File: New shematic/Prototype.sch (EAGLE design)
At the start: 15 parts, among them SW1 1-1825910-4, U1 BOB-12009, U3 NUCLEO-L432KC, U4 24AA64T-I/OT

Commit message: remaked the pcb board
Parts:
- removed JP2, JP3: (no value), pinhead:PINHD-1X1
- added SV2: (no value), con-lstb:MA04-1
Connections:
- removed net N$9: JP2.1, U1.LV, U3G$2.VIN
- new net N$18: SV2.1, SV2.2, U1.LV, U3G$2.VIN
- net GND: now also SV2.3, SV2.4; no longer JP3.1
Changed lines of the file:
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@@
 <part name="GND2" library="supply1" library_urn="urn:adsk.eagle:library:371" deviceset="GND" device=""/>
 <part name="U4" library="24AA64" deviceset="24AA64T-I/OT" device=""/>
-<part name="JP2" library="pinhead" library_urn="urn:adsk.eagle:library:325" deviceset="PINHD-1X1" device="" package3d_urn="urn:adsk.eagle:package:22485/2"/>
-<part name="JP3" library="pinhead" library_urn="urn:adsk.eagle:library:325" deviceset="PINHD-1X1" device="" package3d_urn="urn:adsk.eagle:package:22485/2"/>
 <part name="GND4" library="supply1" library_urn="urn:adsk.eagle:library:371" deviceset="GND" device=""/>
 <part name="P+3" library="supply1" library_urn="urn:adsk.eagle:library:371" deviceset="VCC" device="" value="+3.3V"/>
@@
 <part name="SW1" library="1-1825910-4" deviceset="1-1825910-4" device=""/>
 <part name="U1" library="BOB-12009" deviceset="BOB-12009" device=""/>
+<part name="SV2" library="con-lstb" library_urn="urn:adsk.eagle:library:162" deviceset="MA04-1" device="" package3d_urn="urn:adsk.eagle:package:8337/1"/>
 </parts>
 <sheets>
@@
 <attribute name="VALUE" x="267.7414" y="225.7806" size="2.0828" layer="96" ratio="6" rot="SR90"/>
 </instance>
-<instance part="JP2" gate="G$1" x="149.86" y="116.84" smashed="yes" rot="R180">
-<attribute name="NAME" x="156.21" y="113.665" size="1.778" layer="95" rot="R180"/>
-<attribute name="VALUE" x="156.21" y="121.92" size="1.778" layer="96" rot="R180"/>
-</instance>
-<instance part="JP3" gate="G$1" x="149.86" y="106.68" smashed="yes" rot="R180">
-<attribute name="NAME" x="156.21" y="103.505" size="1.778" layer="95" rot="R180"/>
-<attribute name="VALUE" x="156.21" y="111.76" size="1.778" layer="96" rot="R180"/>
-</instance>
-<instance part="GND4" gate="1" x="165.1" y="101.6" smashed="yes">
-<attribute name="VALUE" x="162.56" y="99.06" size="1.778" layer="96"/>
+<instance part="GND4" gate="1" x="142.24" y="127" smashed="yes" rot="R180">
+<attribute name="VALUE" x="144.78" y="129.54" size="1.778" layer="96" rot="R180"/>
 </instance>
 <instance part="P+3" gate="VCC" x="322.58" y="40.64" smashed="yes" rot="R270">
@@
 <attribute name="NAME" x="58.42" y="173.99" size="1.778" layer="95"/>
 <attribute name="VALUE" x="58.42" y="147.32" size="1.778" layer="96"/>
+</instance>
+<instance part="SV2" gate="1" x="132.08" y="114.3" smashed="yes">
+<attribute name="VALUE" x="130.81" y="104.14" size="1.778" layer="96"/>
+<attribute name="NAME" x="130.81" y="120.142" size="1.778" layer="95"/>
 </instance>
 </instances>
@@
 </segment>
 <segment>
-<pinref part="JP3" gate="G$1" pin="1"/>
-<wire x1="152.4" y1="106.68" x2="165.1" y2="106.68" width="0.1524" layer="91"/>
+<pinref part="SV2" gate="1" pin="4"/>
 <pinref part="GND4" gate="1" pin="GND"/>
-<wire x1="165.1" y1="104.14" x2="165.1" y2="106.68" width="0.1524" layer="91"/>
+<wire x1="139.7" y1="116.84" x2="142.24" y2="116.84" width="0.1524" layer="91"/>
+<wire x1="142.24" y1="116.84" x2="142.24" y2="124.46" width="0.1524" layer="91"/>
+<pinref part="SV2" gate="1" pin="3"/>
+<wire x1="139.7" y1="114.3" x2="142.24" y2="114.3" width="0.1524" layer="91"/>
+<wire x1="142.24" y1="114.3" x2="142.24" y2="116.84" width="0.1524" layer="91"/>
+<junction x="142.24" y="116.84"/>
 </segment>
 </net>
@@
 </segment>
 </net>
-<net name="N$9" class="0">
-<segment>
-<pinref part="U1" gate="G$1" pin="LV"/>
-<wire x1="53.34" y1="170.18" x2="45.72" y2="170.18" width="0.1524" layer="91"/>
-<pinref part="U3" gate="G$2" pin="VIN"/>
-<pinref part="JP2" gate="G$1" pin="1"/>
-<wire x1="198.12" y1="116.84" x2="167.64" y2="116.84" width="0.1524" layer="91"/>
-<wire x1="167.64" y1="116.84" x2="152.4" y2="116.84" width="0.1524" layer="91"/>
-<wire x1="167.64" y1="116.84" x2="167.64" y2="137.16" width="0.1524" layer="91"/>
-<wire x1="167.64" y1="137.16" x2="45.72" y2="137.16" width="0.1524" layer="91"/>
-<junction x="167.64" y="116.84"/>
-<wire x1="45.72" y1="170.18" x2="45.72" y2="137.16" width="0.1524" layer="91"/>
-</segment>
-</net>
 <net name="N$10" class="0">
 <segment>
@@
 </segment>
 </net>
+<net name="N$18" class="0">
+<segment>
+<pinref part="SV2" gate="1" pin="1"/>
+<pinref part="SV2" gate="1" pin="2"/>
+<wire x1="139.7" y1="109.22" x2="139.7" y2="111.76" width="0.1524" layer="91"/>
+<pinref part="U1" gate="G$1" pin="LV"/>
+<wire x1="53.34" y1="170.18" x2="45.72" y2="170.18" width="0.1524" layer="91"/>
+<pinref part="U3" gate="G$2" pin="VIN"/>
+<wire x1="198.12" y1="116.84" x2="167.64" y2="116.84" width="0.1524" layer="91"/>
+<wire x1="167.64" y1="116.84" x2="152.4" y2="116.84" width="0.1524" layer="91"/>
+<wire x1="167.64" y1="116.84" x2="167.64" y2="137.16" width="0.1524" layer="91"/>
+<wire x1="167.64" y1="137.16" x2="45.72" y2="137.16" width="0.1524" layer="91"/>
+<junction x="167.64" y="116.84"/>
+<wire x1="45.72" y1="170.18" x2="45.72" y2="137.16" width="0.1524" layer="91"/>
+<wire x1="139.7" y1="109.22" x2="152.4" y2="109.22" width="0.1524" layer="91"/>
+<wire x1="152.4" y1="109.22" x2="152.4" y2="116.84" width="0.1524" layer="91"/>
+<junction x="139.7" y="109.22"/>
+</segment>
+</net>

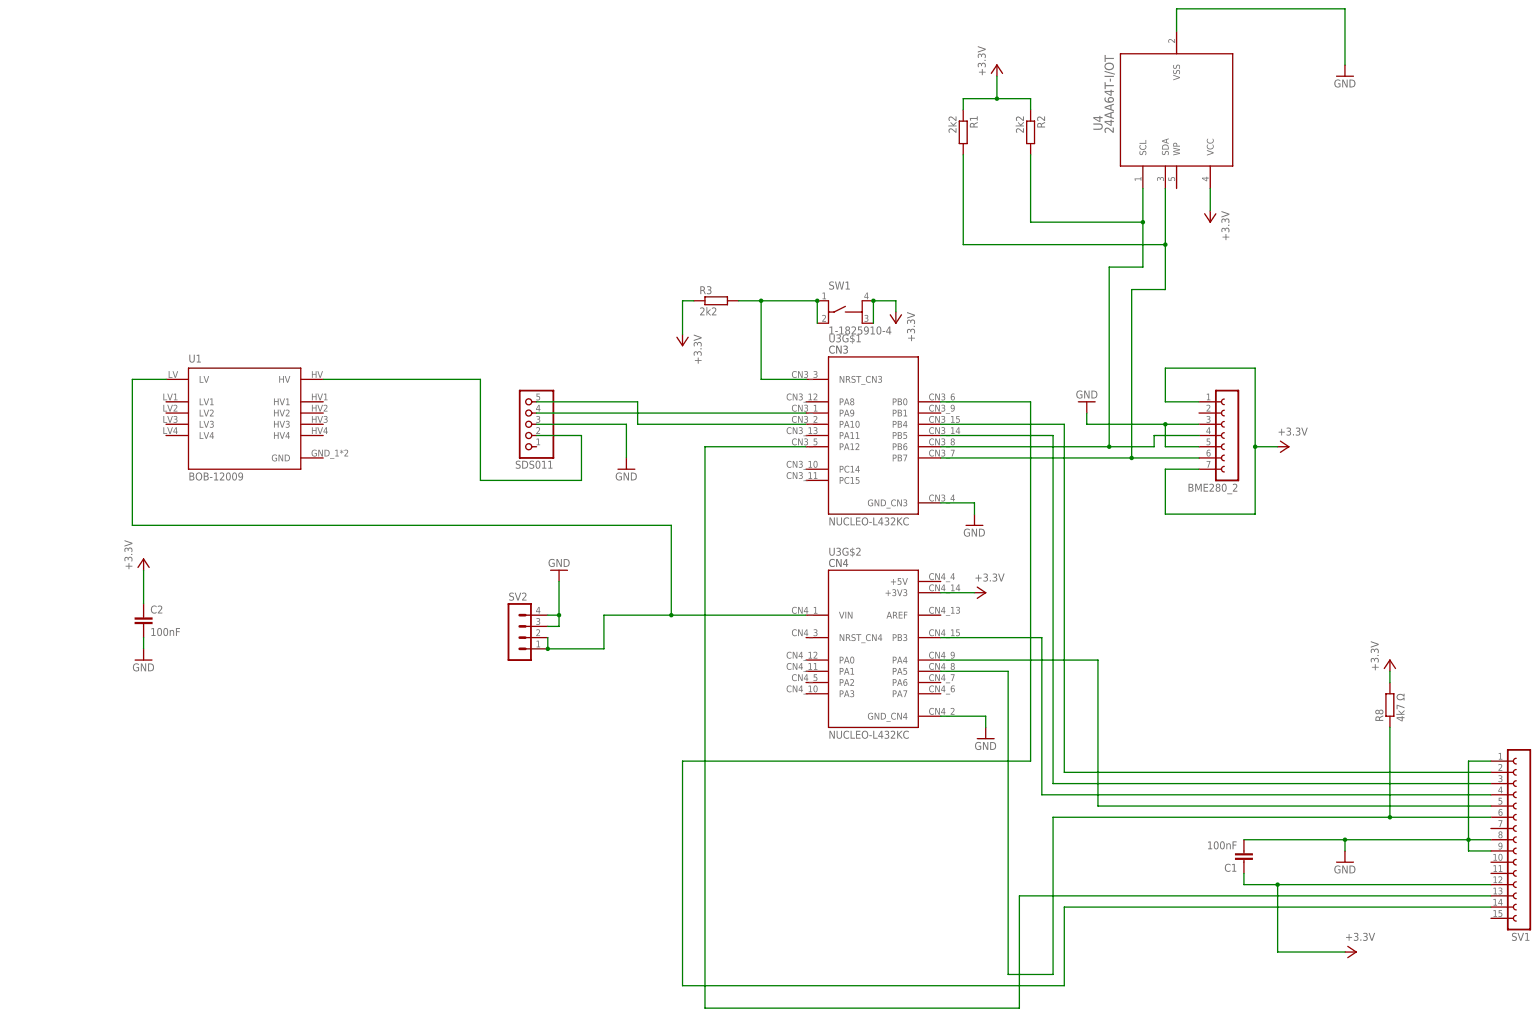
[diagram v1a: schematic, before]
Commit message: refactored the shematic and added components so that sensor can go in sleep
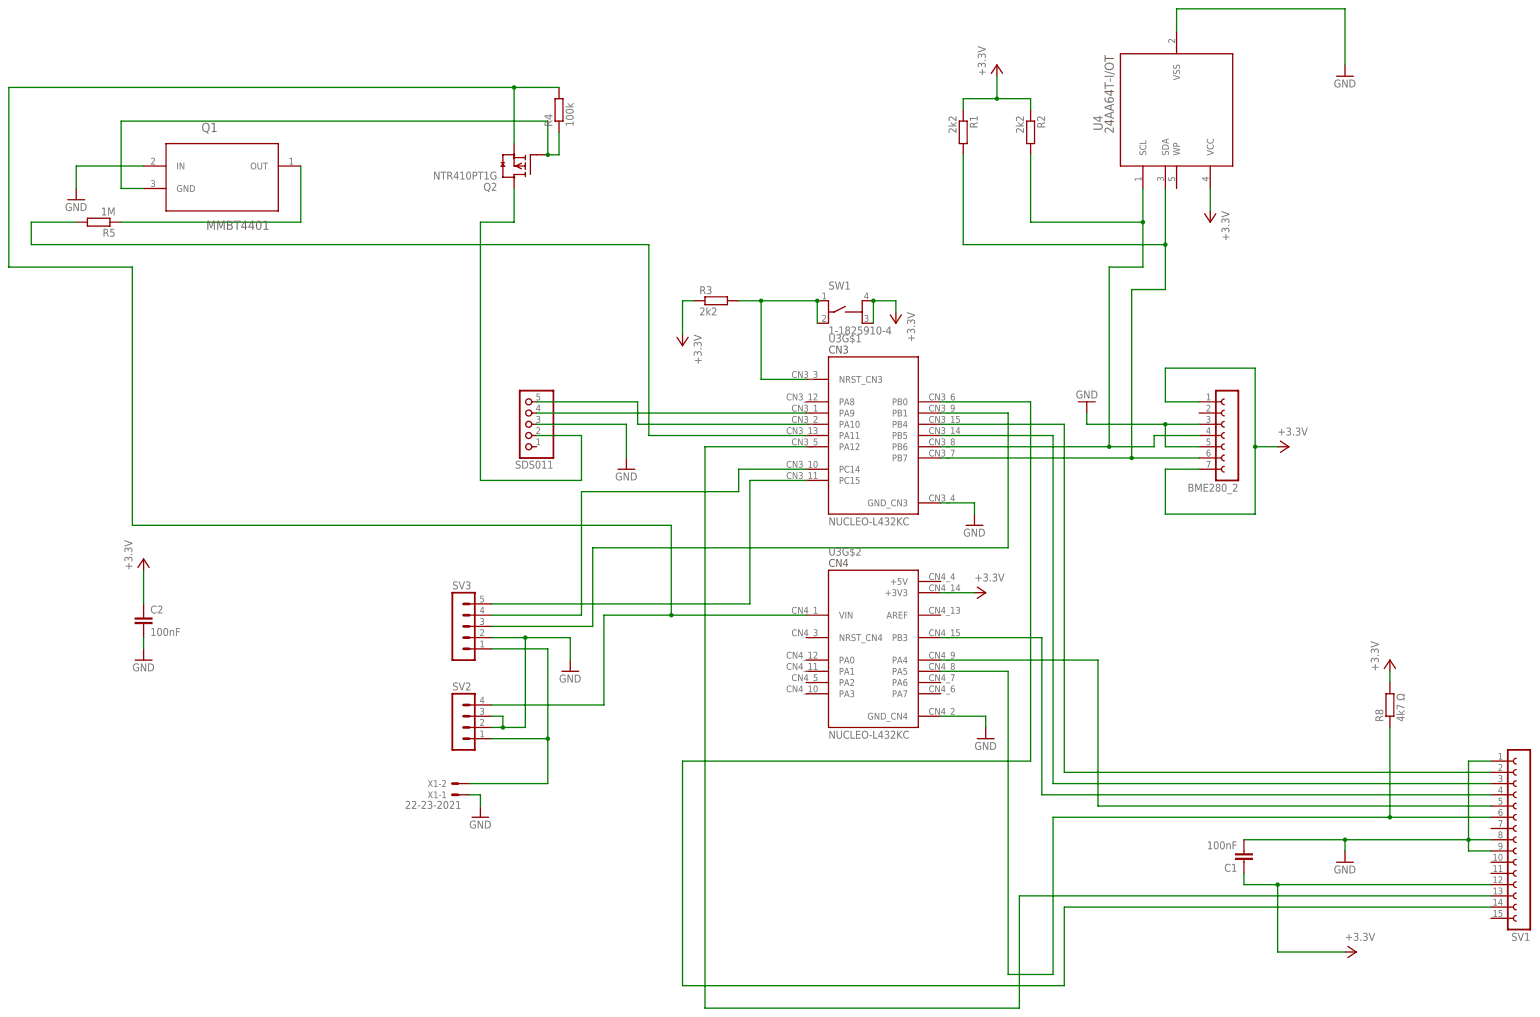
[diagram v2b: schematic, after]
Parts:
- removed U1: BOB-12009, BOB-12009:BOB-12009
- added Q1: MMBT4401, LM3480IM3-5.0:LM3480IM3-5.0
- added Q2: NTR410PT1G, BSS84LT1:BSS84LT1
- added R4: 100k, rcl:R-EU_R1206W
- added R5: 1M, rcl:R-EU_R1206W
- added SV3: (no value), con-lstb:MA05-1
- added X1: 22-23-2021, con-molex:22-23-2021
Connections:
- new net N$21: Q1.OUT, R5.1
- new net N$22: SV2.1, SV3.1, X1-2.S
- new net N$24: SV3.3, U3G$1.PB1
- new net N$25: SV3.4, U3G$1.PC14
- new net N$26: SV3.5, U3G$1.PC15
- new net N$29: R5.2, U3G$1.PA11
- new net N$9: Q1.GND, Q2.G, R4.1
- net GND: now also Q1.IN, SV2.2, SV3.2, X1-1.S; no longer SV2.4
- net N$10: now also Q2.D; no longer U1.HV
- net N$18: now also Q2.S, R4.2, SV2.4; no longer SV2.1, SV2.2, U1.LV
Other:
- moved on the sheet: SV2
